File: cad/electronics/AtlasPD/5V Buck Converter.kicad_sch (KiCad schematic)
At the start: 14 parts, among them J401 Conn_01x04, U401 AMS1117-3.3, U402 AP1509-50SG-13

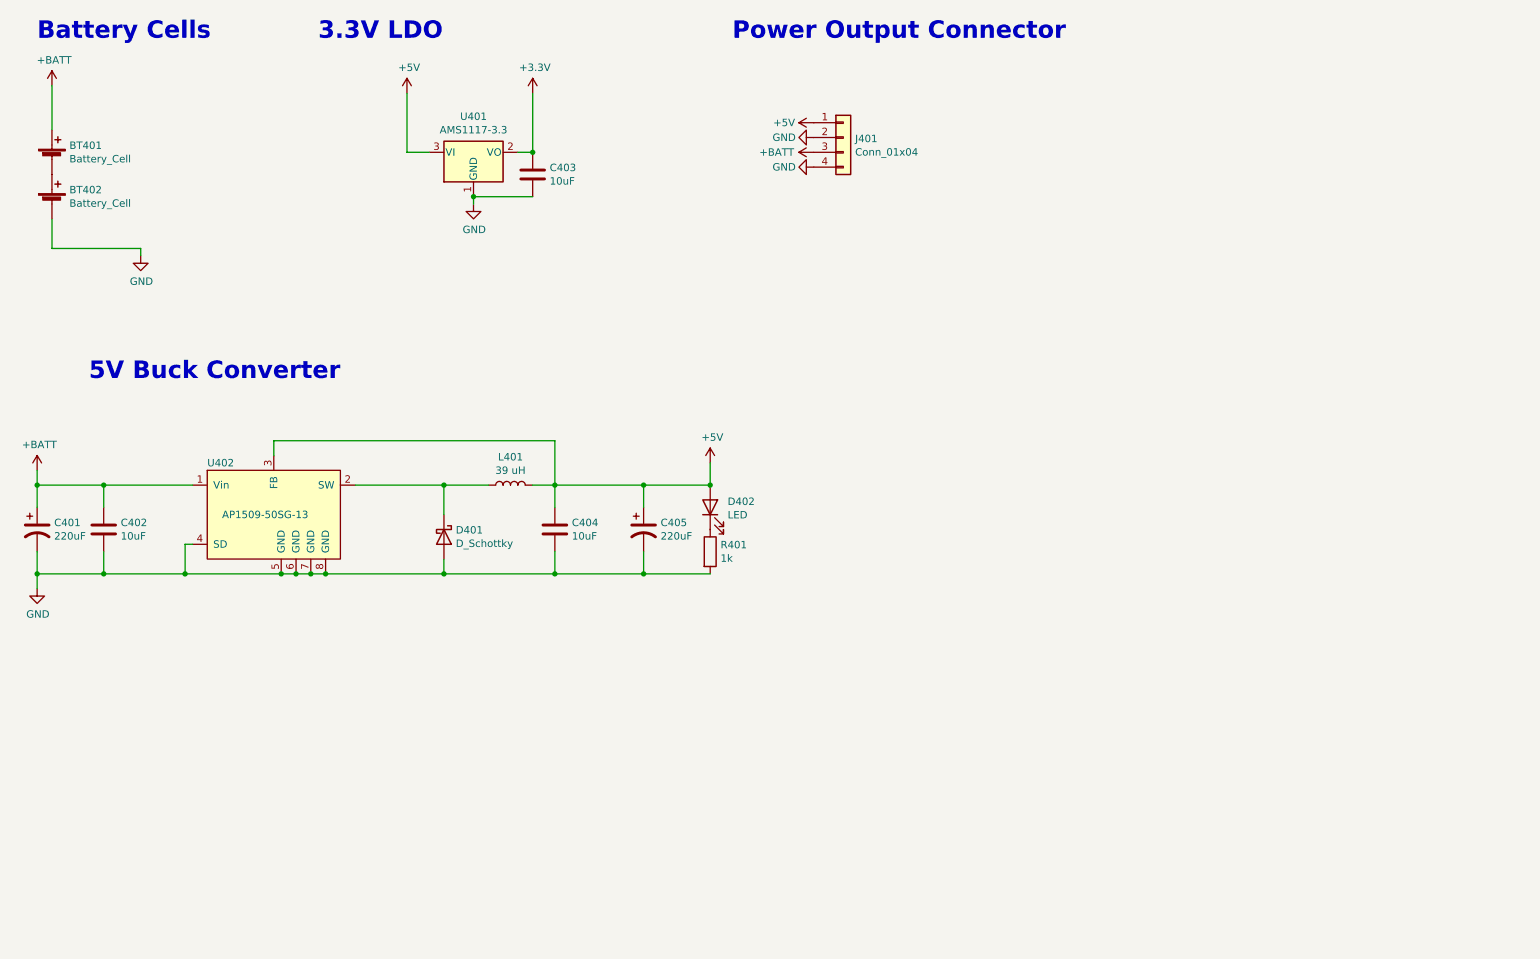
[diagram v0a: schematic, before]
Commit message: Started adding battery protection and fuel guage design
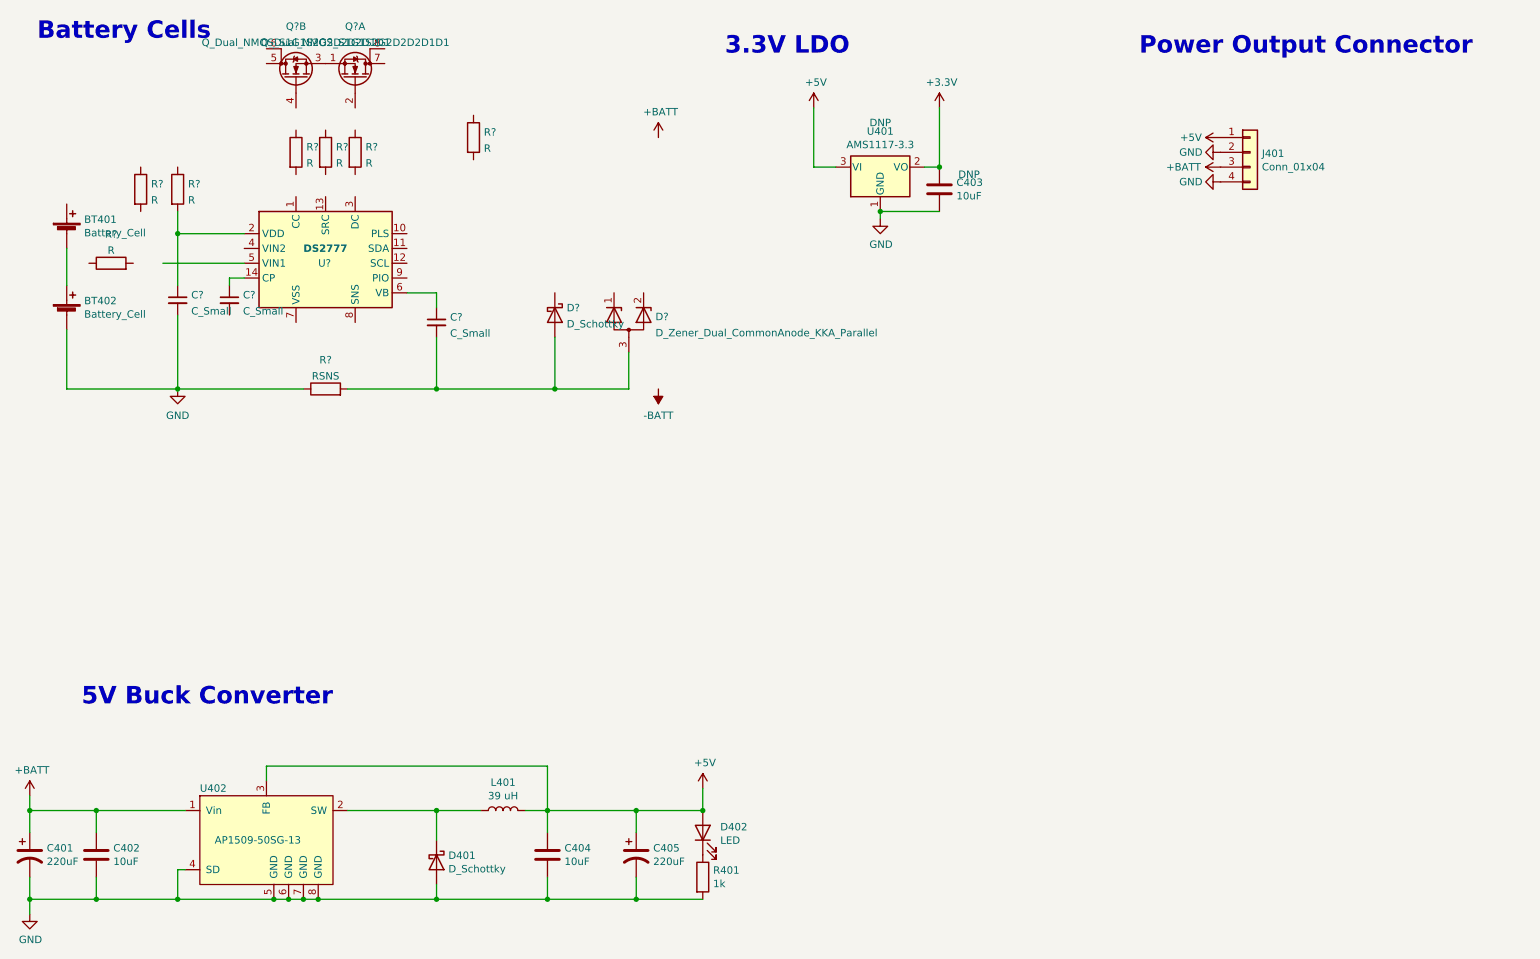
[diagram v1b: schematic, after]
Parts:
- added C? (x3): C_Small, symbol Device:C_Small
- added D?: D_Zener_Dual_CommonAnode_KKA_Parallel, symbol Device:D_Zener_Dual_CommonAnode_KKA_Parallel
- added D?: D_Schottky, symbol Device:D_Schottky
- added Q? (x2): Q_Dual_NMOS_S1G1S2G2D2D2D1D1, symbol Device:Q_Dual_NMOS_S1G1S2G2D2D2D1D1
- added R? (x7): R, symbol Device:R
- added R?: RSNS, symbol Device:R
- added U?: DS2777, symbol SamacSys_Parts:DS2777
- C403, U401: Field4 (none) -> DNP
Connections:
- net +BATT: no longer BT401.1 (+)
- net GND: now also C?.2, R?.1
- new net: C?.2, D?.2 (A), D?.3 (A), R?.2
- new net: C?.1, U?.14 (CP)
- new net: C?.1, R?.2, U?.2 (VDD)
- new net: C?.1, U?.6 (VB)
- new net: Q?.1 (S), Q?.3 (S)
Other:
- moved on the sheet: BT401, BT402, C401, C402, C403, C404, C405, D401, D402, J401, L401, R401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
